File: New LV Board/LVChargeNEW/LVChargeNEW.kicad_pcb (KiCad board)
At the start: 2 copper layers, 44 parts, among them Q1 CSD15380F3T, Q2 CSD15380F3T, Q3 CSD15380F3T, Q4 CSD15380F3T, U1 PQ25856QWRRVRQ1

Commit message: For real this time
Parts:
- added C_sys1: 100u, Capacitor_SMD:C_1210_3225Metric_Pad1.33x2.70mm_HandSolder, F.Cu at (58.4, 107.9)
- added C_sys2: 100u, Capacitor_SMD:C_1210_3225Metric_Pad1.33x2.70mm_HandSolder, F.Cu at (58.4, 112.1)
- added C_sys3: 100u, Capacitor_SMD:C_1210_3225Metric_Pad1.33x2.70mm_HandSolder, F.Cu at (58.4, 116.4)
- added C_sys4: 100u, Capacitor_SMD:C_1210_3225Metric_Pad1.33x2.70mm_HandSolder, F.Cu at (58.6, 78.7)
- added C_sys5: 100u, Capacitor_SMD:C_1210_3225Metric_Pad1.33x2.70mm_HandSolder, F.Cu at (58.6, 82.9)
- added C_sys6: 100u, Capacitor_SMD:C_1210_3225Metric_Pad1.33x2.70mm_HandSolder, F.Cu at (58.6, 87.2)
- added C_sys7: 100u, Capacitor_SMD:C_1210_3225Metric_Pad1.33x2.70mm_HandSolder, F.Cu at (58.4, 92.9)
- added C_sys8: 100u, Capacitor_SMD:C_1210_3225Metric_Pad1.33x2.70mm_HandSolder, F.Cu at (58.4, 97.2)
- added C_sys9: 100u, Capacitor_SMD:C_1210_3225Metric_Pad1.33x2.70mm_HandSolder, F.Cu at (58.4, 101.4)
- added R18: 10k, Resistor_THT:R_Axial_DIN0204_L3.6mm_D1.6mm_P5.08mm_Horizontal, F.Cu at (73.8, 109.3)
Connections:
- net Batt3 renamed Net-(U1-TS)
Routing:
- net Batt-: track 416.0 -> 515.0 mm
- net Batt+: track 49.7 -> 109.3 mm
- net Net-(U1-TS): track 72.7 -> 83.6 mm

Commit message: Added Edge cuts and pins
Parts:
- moved L2 13.4 mm to (154.3, 57.7), turned to 180 degrees
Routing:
- net Net-(U1-SW1): track 260.3 -> 187.4 mm
- net Net-(U1-SW2): track 197.7 -> 193.8 mm
- net (no net): track 1.99 -> 0.00 mm
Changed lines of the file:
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@@
 	(footprint "LVChargeNEWLocalFootprints:SRP1770TA_150M"
 		(layer "F.Cu")
-		(at 167.64 58.42)
+		(at 154.305 57.658 180)
 		(tags "SRP1770TA-150M ")
 		(property "Reference" "L2"
-			(at 0 0 0)
+			(at 0 0 180)
 			(unlocked yes)
 			(layer "F.SilkS")
@@
 		)
 		(property "Value" "SRP1770TA-150M"
-			(at 0 0 0)
+			(at 0 0 180)
 			(unlocked yes)
 			(layer "F.Fab")
@@
 		(attr smd)
 		(fp_line
-			(start -8.7249 -8.7249)
-			(end -8.7249 -6.40334)
+			(start 8.7249 8.7249)
+			(end 8.7249 6.40334)
 			(stroke
 				(width 0.1524)
@@
 		)
 		(fp_line
-			(start -8.7249 6.40334)
-			(end -8.7249 8.7249)
+			(start 8.7249 -6.40334)
+			(end 8.7249 -8.7249)
 			(stroke
 				(width 0.1524)
@@
 		)
 		(fp_line
-			(start -8.7249 8.7249)
-			(end 8.7249 8.7249)
+			(start 8.7249 -8.7249)
+			(end -8.7249 -8.7249)
 			(stroke
 				(width 0.1524)
@@
 		)
 		(fp_line
-			(start 8.7249 -8.7249)
-			(end -8.7249 -8.7249)
+			(start -8.7249 8.7249)
+			(end 8.7249 8.7249)
 			(stroke
 				(width 0.1524)
@@
 		)
 		(fp_line
-			(start 8.7249 -6.40334)
-			(end 8.7249 -8.7249)
+			(start -8.7249 6.40334)
+			(end -8.7249 8.7249)
 			(stroke
 				(width 0.1524)
@@
 		)
 		(fp_line
-			(start 8.7249 8.7249)
-			(end 8.7249 6.40334)
+			(start -8.7249 -8.7249)
+			(end -8.7249 -6.40334)
 			(stroke
 				(width 0.1524)
@@
 		)
 		(fp_line
-			(start -9.5631 -6.3246)
-			(end -8.8519 -6.3246)
+			(start 9.5631 6.3246)
+			(end 8.8519 6.3246)
 			(stroke
 				(width 0.1524)
@@
 		)
 		(fp_line
-			(start -9.5631 6.3246)
-			(end -9.5631 -6.3246)
+			(start 9.5631 -6.3246)
+			(end 9.5631 6.3246)
 			(stroke
 				(width 0.1524)
@@
 		)
 		(fp_line
-			(start -9.5631 6.3246)
-			(end -8.8519 6.3246)
+			(start 9.5631 -6.3246)
+			(end 8.8519 -6.3246)
 			(stroke
 				(width 0.1524)
@@
 		)
 		(fp_line
-			(start -8.8519 -8.8519)
-			(end 8.8519 -8.8519)
+			(start 8.8519 8.8519)
+			(end -8.8519 8.8519)
 			(stroke
 				(width 0.1524)
@@
 		)
 		(fp_line
-			(start -8.8519 -6.3246)
-			(end -8.8519 -8.8519)
+			(start 8.8519 6.3246)
+			(end 8.8519 8.8519)
 			(stroke
 				(width 0.1524)
@@
 		)
 		(fp_line
-			(start -8.8519 8.8519)
-			(end -8.8519 6.3246)
+			(start 8.8519 -8.8519)
+			(end 8.8519 -6.3246)
 			(stroke
 				(width 0.1524)
@@
 		)
 		(fp_line
-			(start 8.8519 -8.8519)
-			(end 8.8519 -6.3246)
+			(start -8.8519 8.8519)
+			(end -8.8519 6.3246)
 			(stroke
 				(width 0.1524)
@@
 		)
 		(fp_line
-			(start 8.8519 6.3246)
-			(end 8.8519 8.8519)
+			(start -8.8519 -6.3246)
+			(end -8.8519 -8.8519)
 			(stroke
 				(width 0.1524)
@@
 		)
 		(fp_line
-			(start 8.8519 8.8519)
-			(end -8.8519 8.8519)
+			(start -8.8519 -8.8519)
+			(end 8.8519 -8.8519)
 			(stroke
 				(width 0.1524)
@@
 		)
 		(fp_line
-			(start 9.5631 -6.3246)
-			(end 8.8519 -6.3246)
+			(start -9.5631 6.3246)
+			(end -8.8519 6.3246)
 			(stroke
 				(width 0.1524)
@@
 		)
 		(fp_line
-			(start 9.5631 -6.3246)
-			(end 9.5631 6.3246)
+			(start -9.5631 6.3246)
+			(end -9.5631 -6.3246)
 			(stroke
 				(width 0.1524)
@@
 		)
 		(fp_line
-			(start 9.5631 6.3246)
-			(end 8.8519 6.3246)
+			(start -9.5631 -6.3246)
+			(end -8.8519 -6.3246)
 			(stroke
 				(width 0.1524)
@@
 		)
 		(fp_line
-			(start -8.5979 -8.5979)
-			(end -8.5979 8.5979)
+			(start 8.5979 8.5979)
+			(end 8.5979 -8.5979)
 			(stroke
 				(width 0.0254)
@@
 		)
 		(fp_line
-			(start -8.5979 8.5979)
-			(end 8.5979 8.5979)
+			(start 8.5979 -8.5979)
+			(end -8.5979 -8.5979)
 			(stroke
 				(width 0.0254)
@@
 		)
 		(fp_line
-			(start 8.5979 -8.5979)
-			(end -8.5979 -8.5979)
+			(start -8.5979 8.5979)
+			(end 8.5979 8.5979)
 			(stroke
 				(width 0.0254)
@@
 		)
 		(fp_line
-			(start 8.5979 8.5979)
-			(end 8.5979 -8.5979)
+			(start -8.5979 -8.5979)
+			(end -8.5979 8.5979)
 			(stroke
 				(width 0.0254)
@@
 		)
 		(fp_text user "${REFERENCE}"
-			(at 0 0 0)
+			(at 0 0 180)
 			(unlocked yes)
 			(layer "F.Fab")
@@
 		)
 		(pad "1" smd rect
-			(at -7.8486 0)
+			(at -7.8486 0 180)
 			(size 2.921 12.1412)
 			(layers "F.Cu" "F.Mask" "F.Paste")
@@
 		)
 		(pad "2" smd rect
-			(at 7.8486 0)
+			(at 7.8486 0 180)
 			(size 2.921 12.1412)
 			(layers "F.Cu" "F.Mask" "F.Paste")
@@
 	)
 	(segment
-		(start 158.0299 60.4101)
-		(end 158.0299 58.42)
-		(width 0.2)
-		(layer "F.Cu")
-		(net 0)
-	)
-	(segment
 		(start 74.36516 62.399)
 		(end 74.681 62.71484)
@@
 	(segment
 		(start 134.62 73.66)
-		(end 154.94 73.66)
+		(end 145.669 73.66)
 		(width 0.2)
 		(layer "F.Cu")
@@
 	)
 	(segment
+		(start 145.669 73.66)
+		(end 146.4564 72.8726)
+		(width 0.2)
+		(layer "F.Cu")
+		(net 10)
+	)
+	(segment
 		(start 143.042 113.5102)
 		(end 142.422835 114.129365)
@@
 	)
 	(segment
-		(start 147.32 38.1)
-		(end 134.62 50.8)
-		(width 0.2)
-		(layer "F.Cu")
-		(net 10)
-	)
-	(segment
 		(start 121.595 112.8048)
 		(end 121.595 110.67)
@@
 	)
 	(segment
-		(start 175.4886 58.42)
-		(end 175.4886 38.3286)
-		(width 0.2)
-		(layer "F.Cu")
-		(net 10)
-	)
-	(segment
 		(start 142.422835 114.130778)
 		(end 142.070778 114.482835)
@@
 	)
 	(segment
-		(start 175.26 38.1)
-		(end 147.32 38.1)
-		(width 0.2)
-		(layer "F.Cu")
-		(net 10)
-	)
-	(segment
 		(start 129.54 101.6)
 		(end 129.941 101.199)
@@
 	)
 	(segment
-		(start 134.62 50.8)
-		(end 134.62 73.66)
-		(width 0.2)
-		(layer "F.Cu")
-		(net 10)
-	)
-	(segment
-		(start 175.4886 38.3286)
-		(end 175.26 38.1)
-		(width 0.2)
-		(layer "F.Cu")
-		(net 10)
-	)
-	(segment
 		(start 145.442 103.822722)
 		(end 145.442 109.6922)
@@
 	)
 	(segment
+		(start 146.4564 72.8726)
+		(end 146.4564 57.658)
+		(width 0.2)
+		(layer "F.Cu")
+		(net 10)
+	)
+	(segment
+		(start 145.669 73.66)
+		(end 154.94 73.66)
+		(width 0.2)
+		(layer "F.Cu")
+		(net 10)
+	)
+	(segment
 		(start 134.219 101.199)
 		(end 134.62 101.6)
@@
 		(width 0.2)
 		(layer "F.Cu")
-		(net 11)
-	)
-	(segment
-		(start 159.7914 58.42)
-		(end 162.56 61.1886)
-		(width 0.2)
-		(layer "F.Cu")

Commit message: updated LVCharge
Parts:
- added J1: Conn_01x04_Socket, Connector_PinSocket_1.27mm:PinSocket_1x04_P1.27mm_Vertical, F.Cu at (80.0, 50.8)
- added J2: Conn_01x05_Socket, Connector_PinSocket_1.27mm:PinSocket_1x06_P1.27mm_Vertical, F.Cu at (120.7, 50.8)
- moved C_sys9 25.2 mm to (58.4, 76.2)
- moved C_sys4 22.9 mm to (58.4, 101.6)
- moved C_sys8 15.9 mm to (58.4, 81.3)
- moved C_sys5 13.6 mm to (58.4, 96.5)
- moved C7 10.2 mm to (81.3, 81.3)
- moved C_sys3 9.71 mm to (58.4, 106.7)
- moved C_sys1 8.95 mm to (58.4, 116.8)
- moved C_sys7 6.55 mm to (58.4, 86.4)
- moved C_sys6 4.26 mm to (58.4, 91.4)
- moved C5 3.59 mm to (66.1, 76.2)
- moved L2 3.30 mm to (154.3, 61.0)
- moved C8 2.62 mm to (71.0, 88.9)
- moved C1 2.54 mm to (71.0, 63.5)
- moved C_sys2 0.38 mm to (58.4, 111.8)
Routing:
- net CE: track 0.00 -> 135.5 mm, vias 0 -> 1
- net Batt+: track 109.3 -> 236.6 mm
- net Batt-: track 515.0 -> 601.6 mm
- net SCL: track 0.00 -> 84.7 mm, vias 0 -> 1
- net SDL: track 0.00 -> 82.4 mm, vias 0 -> 1
- net INT: track 0.00 -> 79.4 mm, vias 0 -> 1
- net Net-(C9-Pad2): track 73.8 -> 61.4 mm
- net Net-(U1-LODRV1): track 94.8 -> 82.9 mm, vias 2 -> 0
- net Buck Input: track 153.4 -> 162.0 mm
- net Net-(U1-ACN): track 194.4 -> 189.0 mm
- net Net-(U1-BTST1): track 92.0 -> 86.9 mm
- net Net-(U1-SW1): track 187.4 -> 184.2 mm, vias 3 -> 2
- net Net-(U1-SW2): track 193.8 -> 191.8 mm
- net Net-(U1-TS): track 83.6 -> 85.3 mm
- net Net-(U1-ACP): track 106.6 -> 107.6 mm
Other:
- board outline added: 137.2 x 96.5 mm
- board text added: "LV Charge Circuit Lafayette Motorsports Sean McLoughlin, Robin Stopford"

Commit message: update lvcharge
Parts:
- moved Q1 4.25 mm to (126.0, 110.3)
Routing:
- net Net-(U1-ACN): track 189.0 -> 163.9 mm
- net Net-(D1-A): track 210.5 -> 190.1 mm
- net Net-(U1-HIDRV1): track 102.1 -> 96.0 mm
- net Batt-: track 601.6 -> 596.8 mm
- net Net-(U1-SW2): track 191.8 -> 186.9 mm, vias 2 -> 1
- net Buck Input: track 162.0 -> 166.6 mm
- net Net-(C12-Pad2): track 76.1 -> 72.0 mm
- net Net-(U1-SW1): track 184.2 -> 180.5 mm
- net Net-(U1-SRN): track 123.1 -> 125.3 mm
- net Batt+: track 236.6 -> 238.3 mm

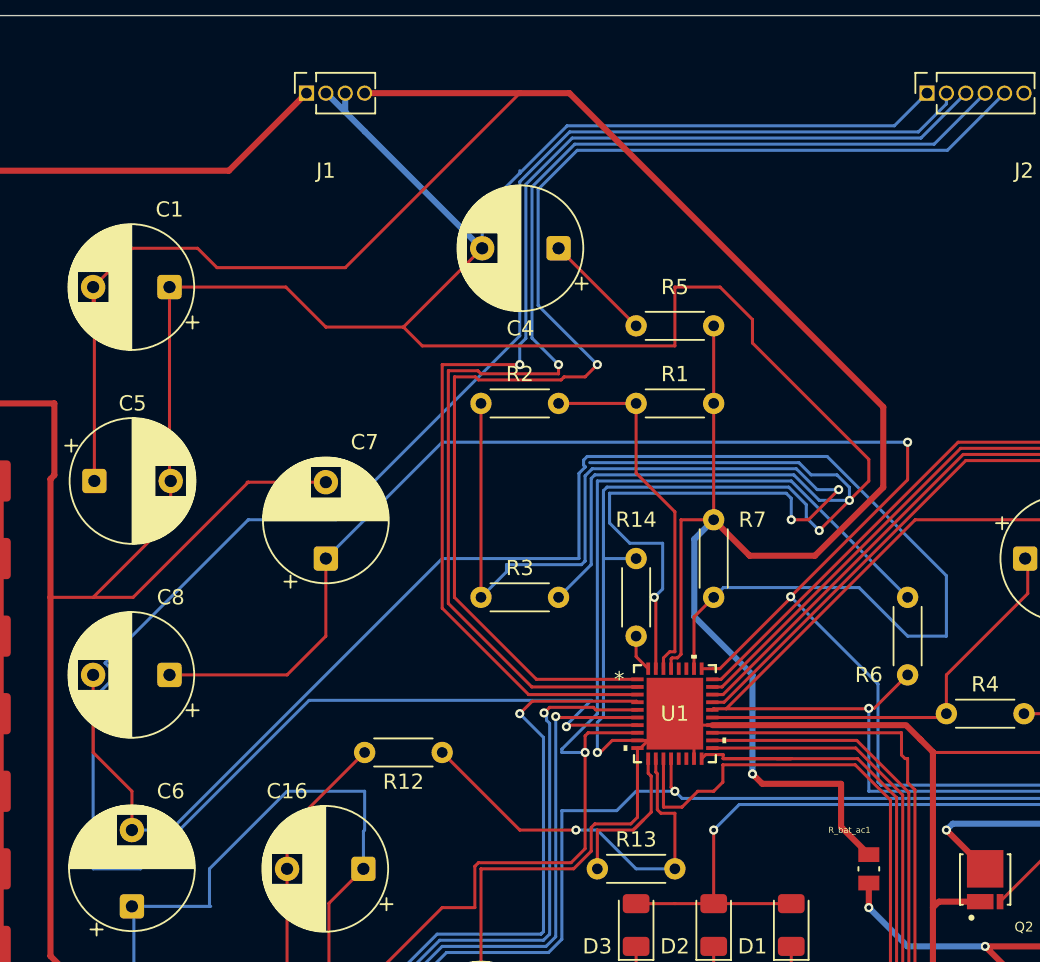
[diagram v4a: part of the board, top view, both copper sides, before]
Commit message: add Ichg limit resistor
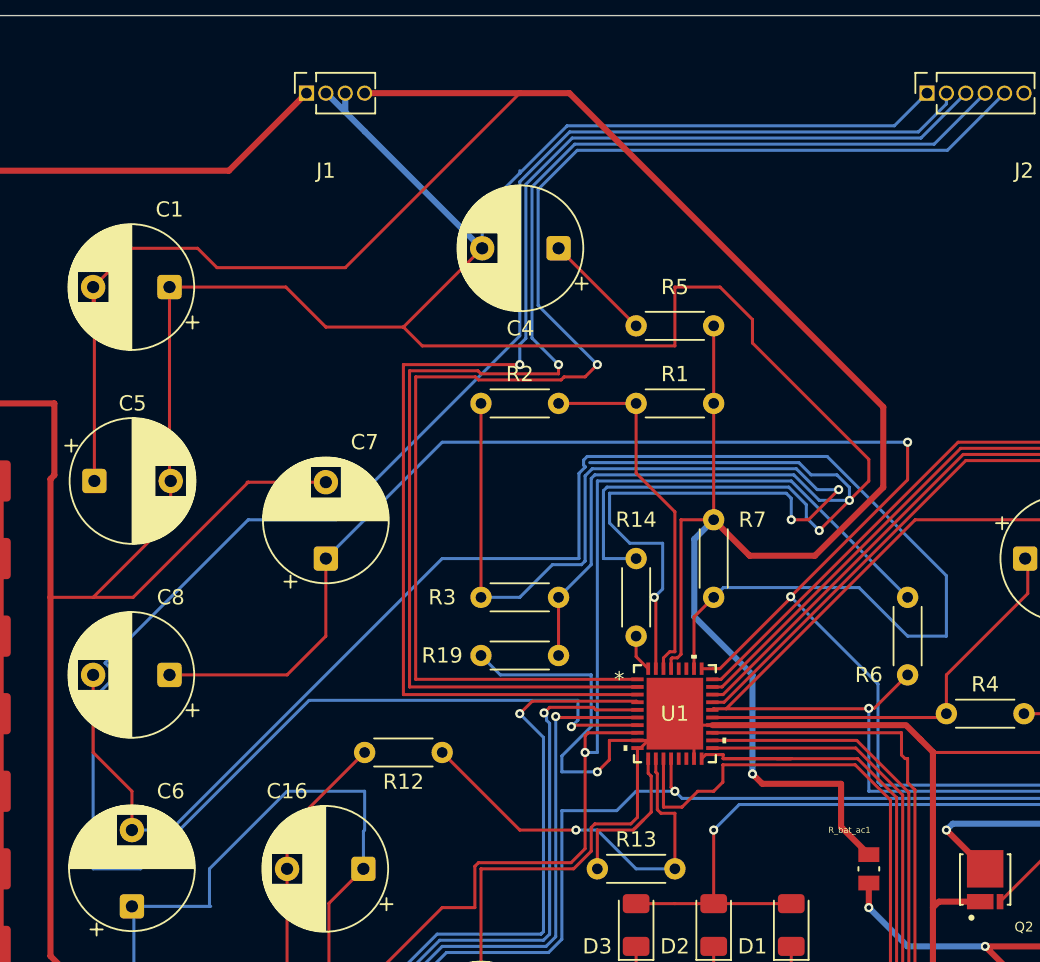
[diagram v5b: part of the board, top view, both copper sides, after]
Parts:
- added R19: 2.6K, Resistor_THT:R_Axial_DIN0204_L3.6mm_D1.6mm_P5.08mm_Horizontal, F.Cu at (91.4, 87.6)
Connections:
- U1 pad 9: Batt- -> Net-(U1-ICHG)
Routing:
- net Net-(U1-ICHG): track 0.00 -> 21.0 mm, vias 0 -> 1
- net Batt-: track 596.8 -> 584.8 mm, vias 3 -> 2
- net INT: track 79.4 -> 87.8 mm
- net SDL: track 82.4 -> 90.7 mm
- net SCL: track 84.7 -> 93.0 mm
- net CE: track 135.5 -> 133.8 mm
- net Net-(U1-TS): track 85.3 -> 83.6 mm

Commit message: up
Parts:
- added R20: 249k, Resistor_THT:R_Axial_DIN0204_L3.6mm_D1.6mm_P5.08mm_Horizontal, F.Cu at (55.9, 66.0)
- moved C8 2.87 mm to (73.9, 88.9)
- moved R5 1.78 mm to (108.5, 66.0)
- moved C4 0.28 mm to (96.6, 60.7)
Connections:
- C_sys1 pad 1: Batt- -> Net-(C_sys1-Pad1)
- C_sys2 pad 1: Batt- -> Net-(C_sys1-Pad1)
- C_sys3 pad 1: Batt- -> Net-(C_sys1-Pad1)
- C_sys4 pad 1: Batt- -> Net-(C_sys1-Pad1)
- C_sys5 pad 1: Batt- -> Net-(C_sys1-Pad1)
- C_sys6 pad 1: Batt- -> Net-(C_sys1-Pad1)
- C_sys7 pad 1: Batt- -> Net-(C_sys1-Pad1)
- C_sys8 pad 1: Batt- -> Net-(C_sys1-Pad1)
- C_sys9 pad 1: Batt- -> Net-(C_sys1-Pad1)
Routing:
- net Batt-: track 584.8 -> 707.9 mm, vias 2 -> 4
- net Net-(C_sys1-Pad1): track 0.00 -> 51.2 mm
- net Net-(C9-Pad2): track 61.7 -> 72.0 mm
- net Net-(U1-SW1): track 180.5 -> 170.2 mm
- net CE: track 133.8 -> 140.9 mm
- net SCL: track 93.0 -> 86.9 mm
- net SDL: track 90.7 -> 87.6 mm
- net Net-(U1-ACN): track 163.9 -> 161.0 mm
- net Net-(U1-HIDRV1): track 96.0 -> 93.3 mm
- net Net-(C4-Pad1): track 7.18 -> 8.96 mm
- net Net-(U1-ACP): track 107.6 -> 106.7 mm
- net Net-(U1-FBG): track 10.9 -> 10.1 mm
- net Buck Input: track 166.6 -> 166.1 mm
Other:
- board text added: "1"
- board text added: "2"
- board text added: "3"
- board text added: "4"
- board text added: "5"
- board text added: "6"
- board text added: "I2C"
- board text added: "I2c: 1: Gnd 2: CE 3: INT 4: SDL 5: SCL"
- board text added: "Power"
- board text added: "Power: 1: Batt+ 2: Gnd 3: Gnd 4: Buck+"

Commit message: up!
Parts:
- added J3: Conn_01x05_Socket, Connector_PinSocket_1.27mm:PinSocket_1x06_P1.27mm_Vertical, F.Cu at (120.7, 50.3)
- J1: value Conn_01x04_Socket -> Conn_01x02; footprint Connector_PinSocket_1.27mm:PinSocket_1x04_P1.27mm_Vertical -> TerminalBlock:TerminalBlock_Xinya_XY308-2.54-2P_1x02_P2.54mm_Horizontal
- J2: value Conn_01x05_Socket -> Conn_01x02; footprint Connector_PinSocket_1.27mm:PinSocket_1x06_P1.27mm_Vertical -> TerminalBlock:TerminalBlock_Xinya_XY308-2.54-2P_1x02_P2.54mm_Horizontal
- moved J2 47.5 mm to (73.2, 51.1), turned to 0 degrees
- moved J1 22.9 mm to (57.1, 51.1), turned to 0 degrees
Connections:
- J2 pad 2: CE -> Buck Input
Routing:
- net Batt+: track 238.3 -> 215.4 mm
- net Batt-: track 707.9 -> 715.8 mm, vias 4 -> 5
- net Buck Input: track 166.1 -> 160.7 mm
- net Net-(U1-ACP): track 106.7 -> 103.4 mm

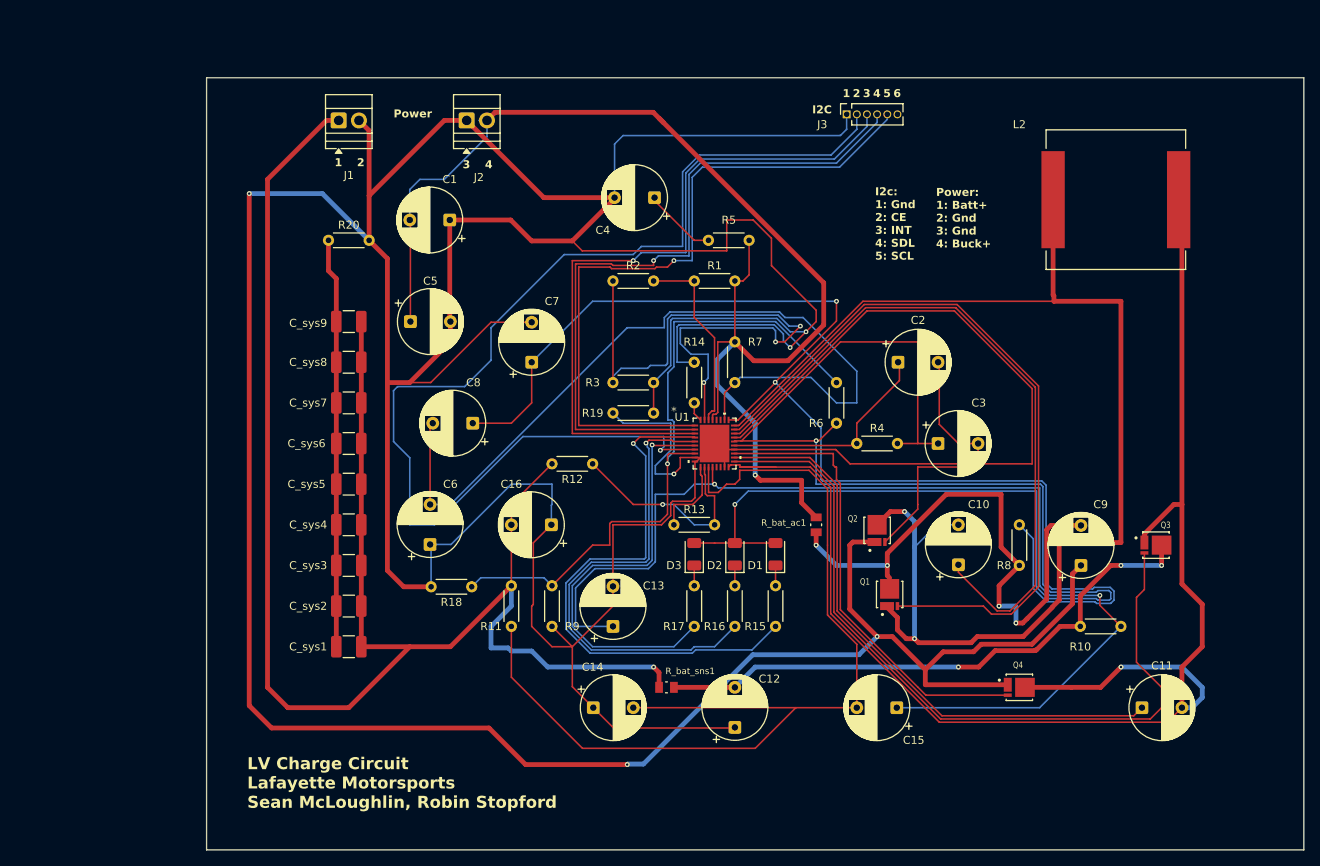
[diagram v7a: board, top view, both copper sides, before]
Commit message: added pins to glv charge
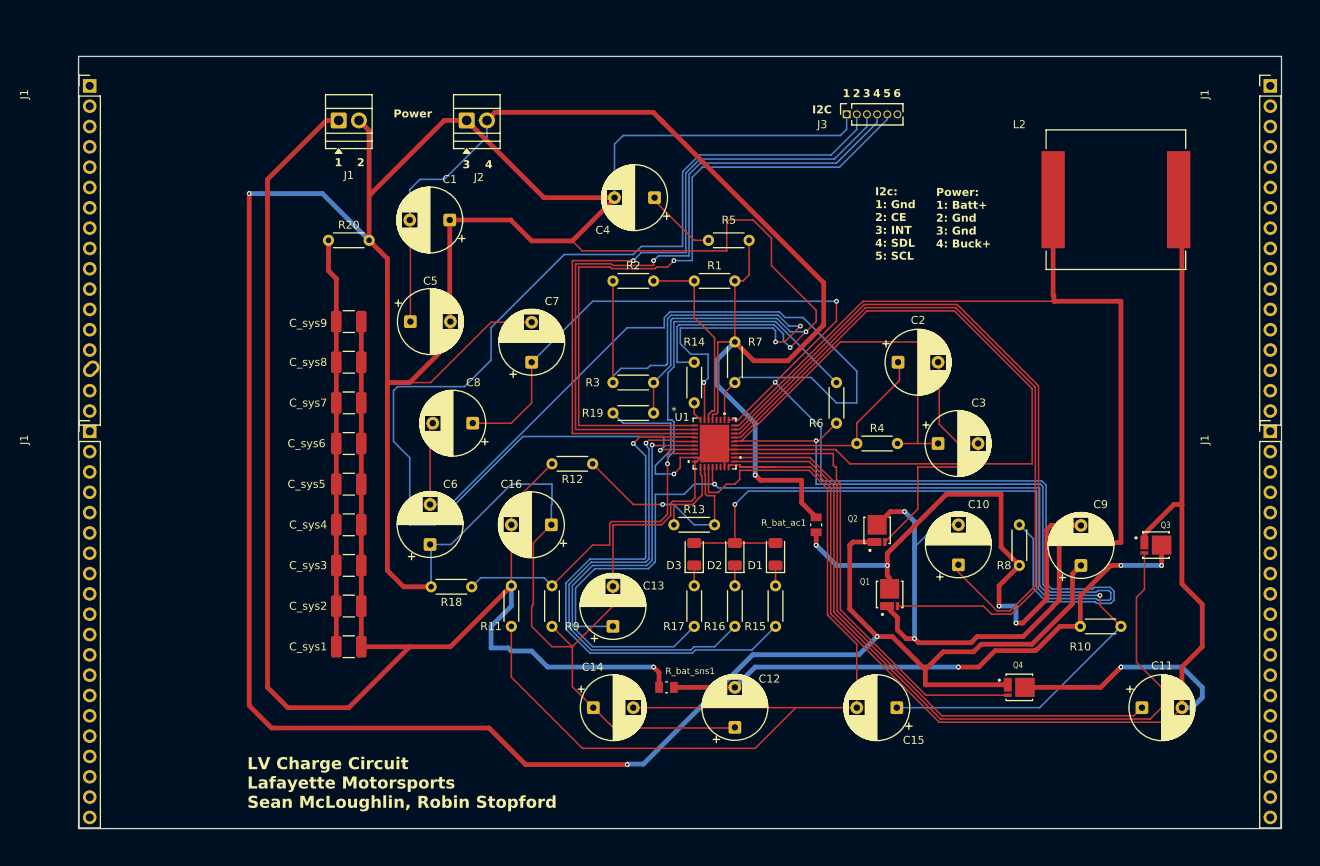
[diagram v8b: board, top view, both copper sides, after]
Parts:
- added ?: , , F.Cu at (26.4, 81.9)
- added J1: PH1-20-UA, Connector_PinHeader_2.54mm:PinHeader_1x20_P2.54mm_Vertical, F.Cu at (26.0, 89.9)
- added J1: PH1-20-UA, Connector_PinHeader_2.54mm:PinHeader_1x20_P2.54mm_Vertical, F.Cu at (173.6, 46.7)
- added J1: PH1-20-UA, Connector_PinHeader_2.54mm:PinHeader_1x20_P2.54mm_Vertical, F.Cu at (26.0, 46.7)
- added J1: PH1-20-UA, Connector_PinHeader_2.54mm:PinHeader_1x20_P2.54mm_Vertical, F.Cu at (173.6, 89.9)
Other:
- board size 137.2 x 96.5 mm -> 150.4 x 96.5 mm
